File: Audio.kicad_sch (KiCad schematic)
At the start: 25 parts, among them J4 AudioJack3, J5 AudioJack3_SwitchT, U2 MAX9850xTI, U3 TPA6132A2RTE

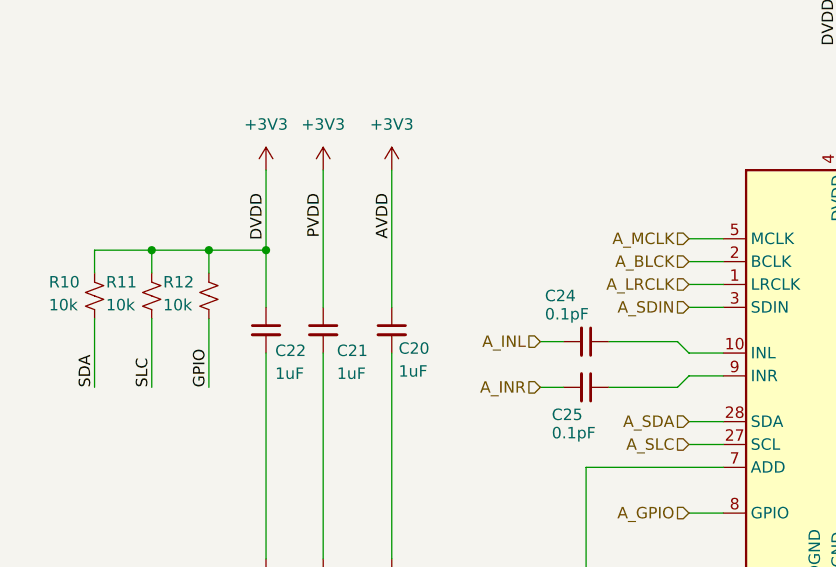
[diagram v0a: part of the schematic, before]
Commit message: Draft 1 - Main components and wiring complete
Connections may be innacurate or violate electrical specs, or perhaps aren't set up "properly".
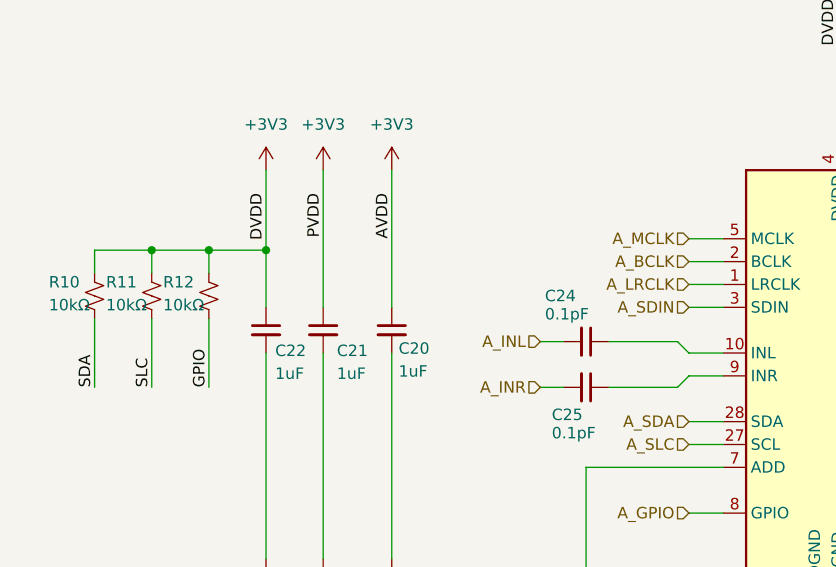
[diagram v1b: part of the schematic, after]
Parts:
- R10, R11, R12: value 10k -> 10kΩ
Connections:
- net A_BLCK renamed A_BCLK
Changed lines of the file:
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@@
 		)
 	)
-	(hierarchical_label "A_BLCK"
+	(hierarchical_label "A_BCLK"
 		(shape input)
 		(at 99.06 71.12 180)
@@
 			)
 		)
-		(property "Value" "10k"
+		(property "Value" "10kΩ"
 			(at 40.64 75.946 0)
 			(effects
@@
 			)
 		)
-		(property "Value" "10k"
+		(property "Value" "10kΩ"
 			(at 34.29 75.946 0)
 			(effects
@@
 			)
 		)
-		(property "Value" "10k"
+		(property "Value" "10kΩ"
 			(at 27.94 75.946 0)
 			(effects

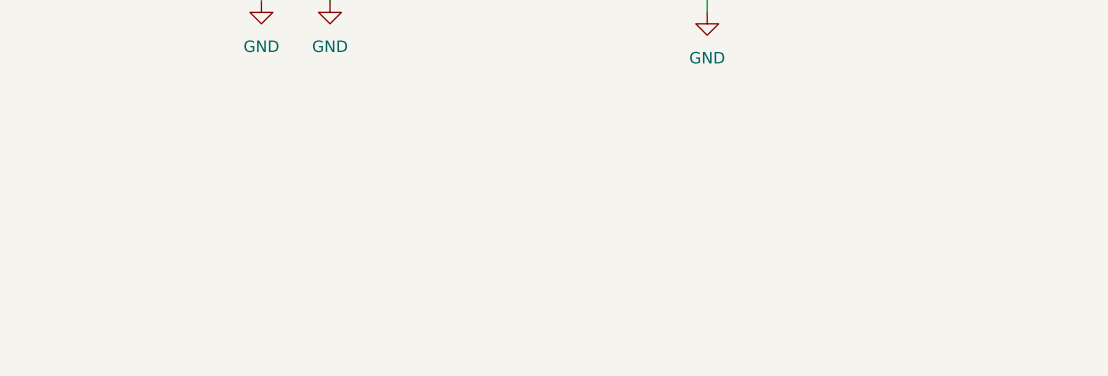
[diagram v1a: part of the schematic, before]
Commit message: Added missing datasheets.
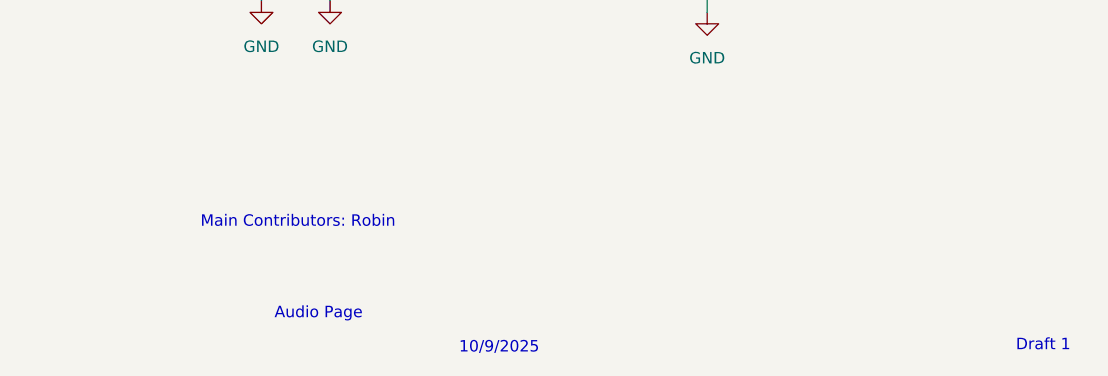
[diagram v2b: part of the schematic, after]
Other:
- note added: "10/9/2025"
- note added: "Audio Page"
- note added: "Draft 1"
- note added: "Main Contributors: Robin"
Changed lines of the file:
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@@
+		)
+	)
+	(text "Audio Page"
+		(exclude_from_sim no)
+		(at 191.77 189.738 0)
+		(effects
+			(font
+				(size 1.27 1.27)
+			)
 		)
 	)
@@
 				(thickness 0.508)
 				(bold yes)
+			)
+		)
+	)
+	(text "Main Contributors: Robin"
+		(exclude_from_sim no)
+		(at 189.484 179.578 0)
+		(effects
+			(font
+				(size 1.27 1.27)
 			)
 		)
@@
 		)
 	)
+	(text "Draft 1"
+		(exclude_from_sim no)
+		(at 272.288 193.294 0)
+		(effects
+			(font
+				(size 1.27 1.27)
+			)
+		)
+	)
 	(text "Place near VDD"
 		(exclude_from_sim no)
@@
 		(effects
 			(font
+				(size 1.27 1.27)
+			)
+		)
+	)
+	(text "10/9/2025"
+		(exclude_from_sim no)
+		(at 211.836 193.548 0)
+		(effects
+			(font

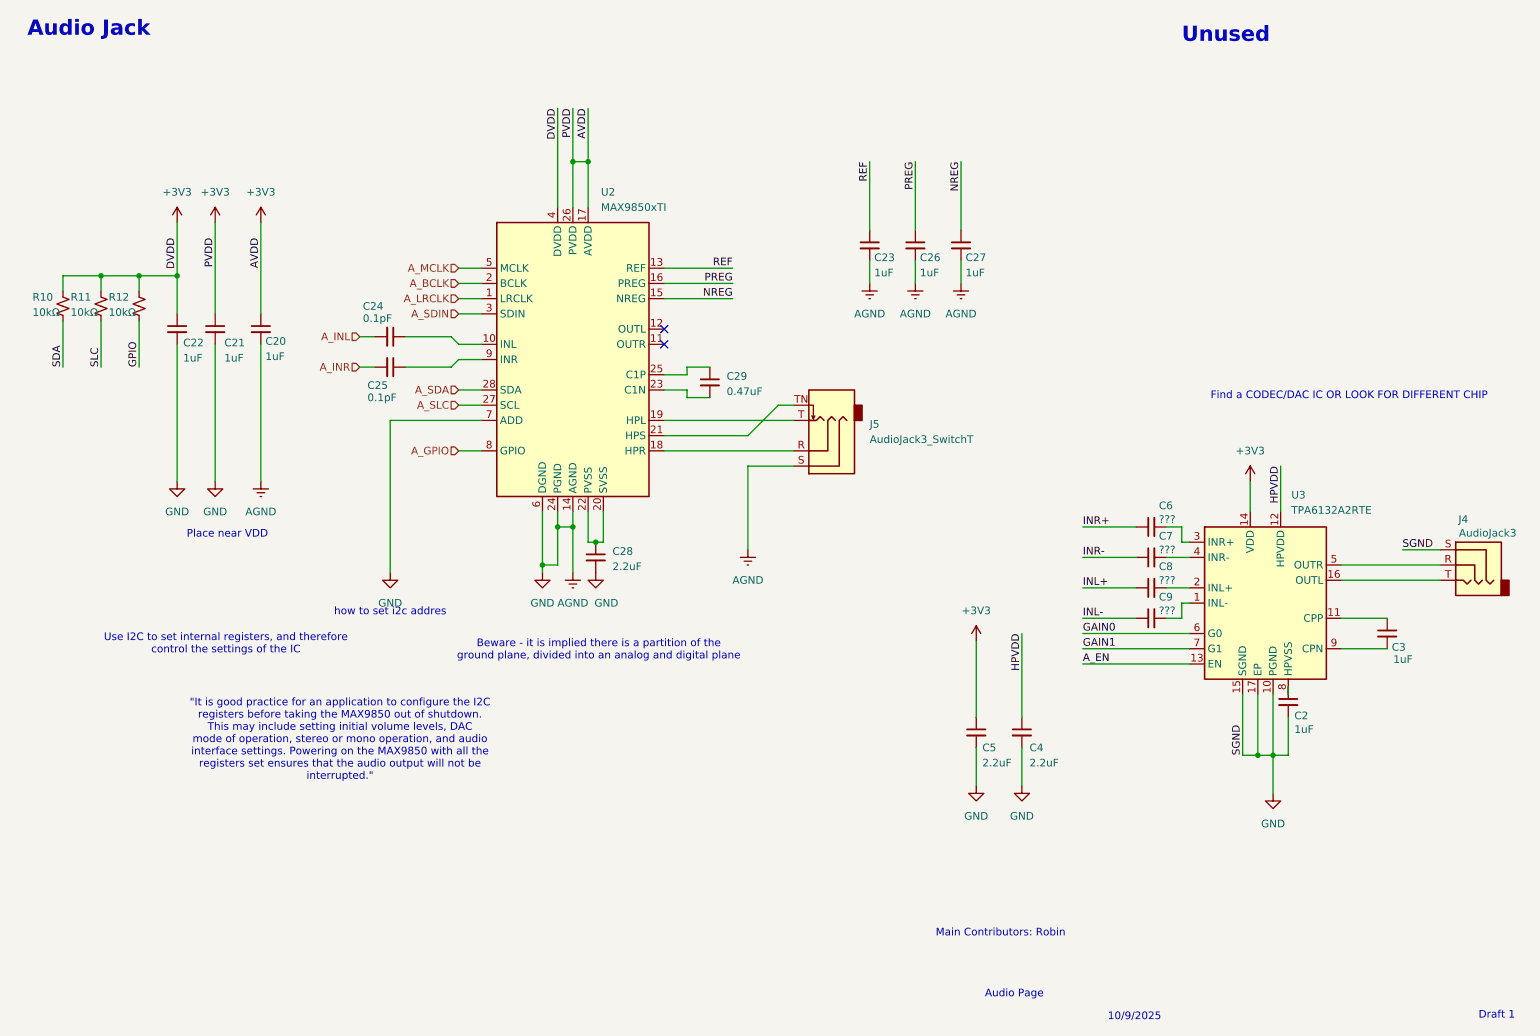
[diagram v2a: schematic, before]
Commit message: Added PMOS to battery + power flags
Still missing values for a lot of components
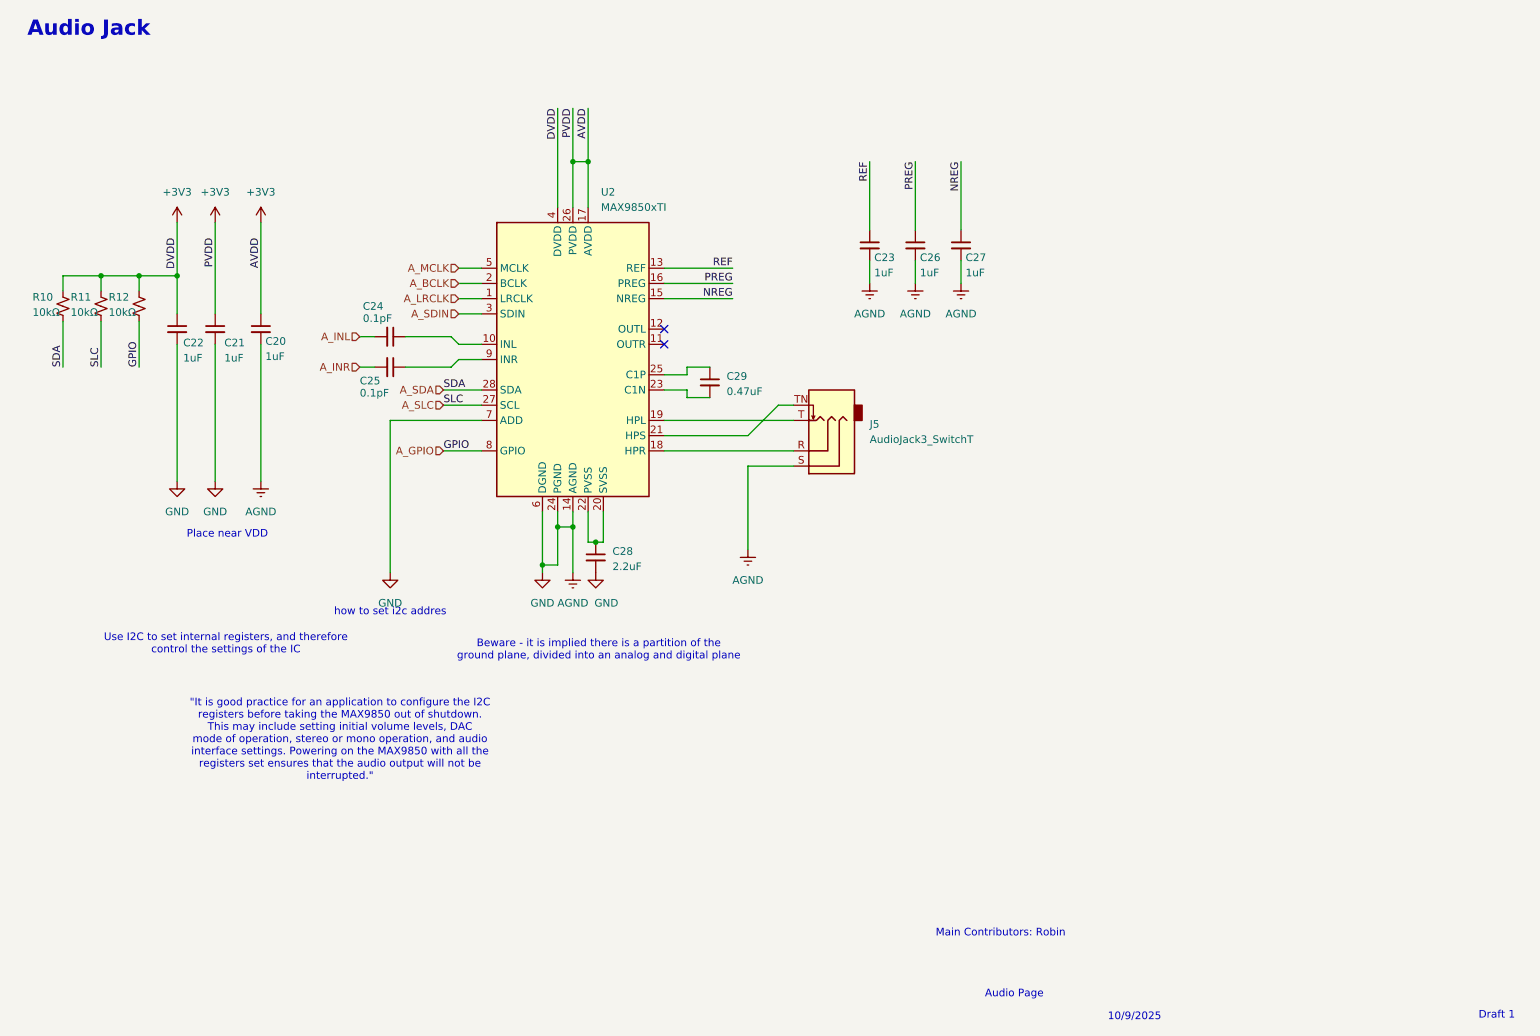
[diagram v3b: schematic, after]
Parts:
- removed C2, C3: 1uF, symbol Device:C_Small
- removed C4, C5: 2.2uF, symbol Device:C_Small
- removed C6, C7, C8, C9: ???, symbol Device:C_Small
- removed J4: AudioJack3, symbol Connector_Audio:AudioJack3
- removed U3: TPA6132A2RTE, Package_DFN_QFN:WQFN-16-1EP_3x3mm_P0.5mm_EP1.6x1.6mm_ThermalVias, symbol Amplifier_Audio:TPA6132A2RTE
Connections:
- net GPIO is gone; now on net A_GPIO: R12.2
- net SDA is gone; now on net A_SDA: R10.2
- net SLC is gone; now on net A_SLC: R11.2
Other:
- note removed: "Find a CODEC/DAC IC OR LOOK FOR DIFFERENT CHIP"
- note removed: "Unused"

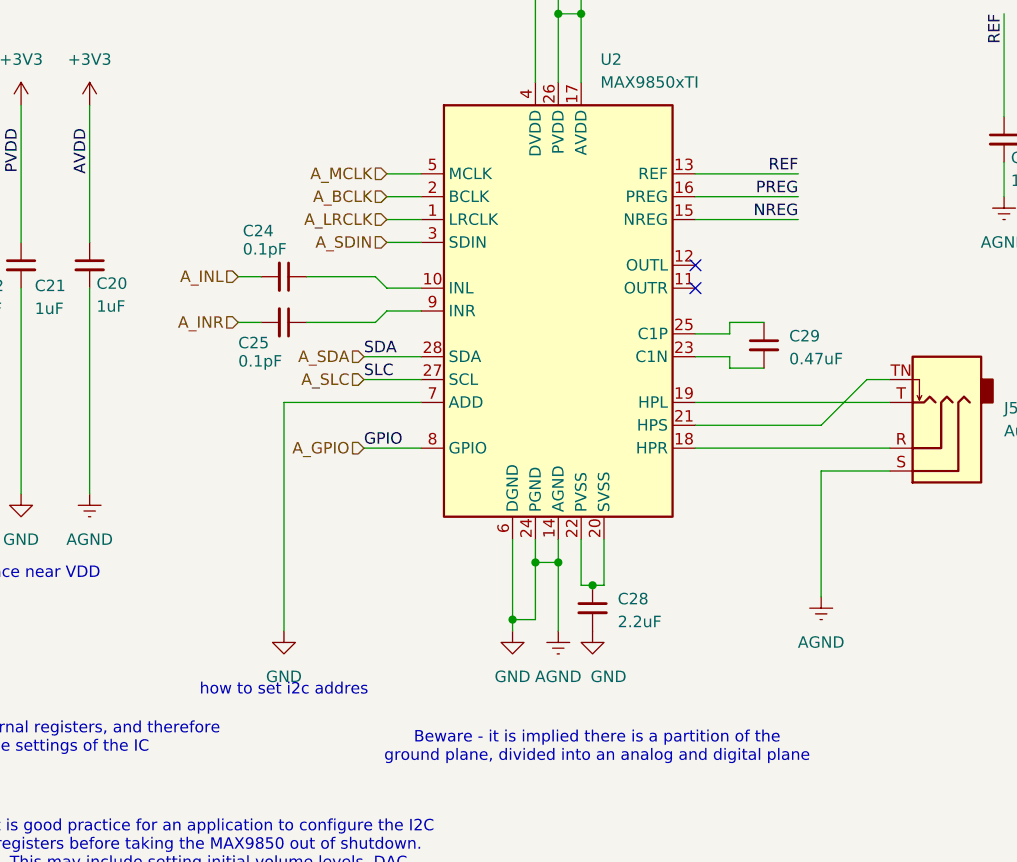
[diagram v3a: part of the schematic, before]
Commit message: Draft 2: Protection circuitry and fixed I/O signals
Still missing PMOS spec for reverse polarity battery protection. Added TVS to USB, voltage divided certain output signals from ICs into ESP GPIO. Checked some component values.
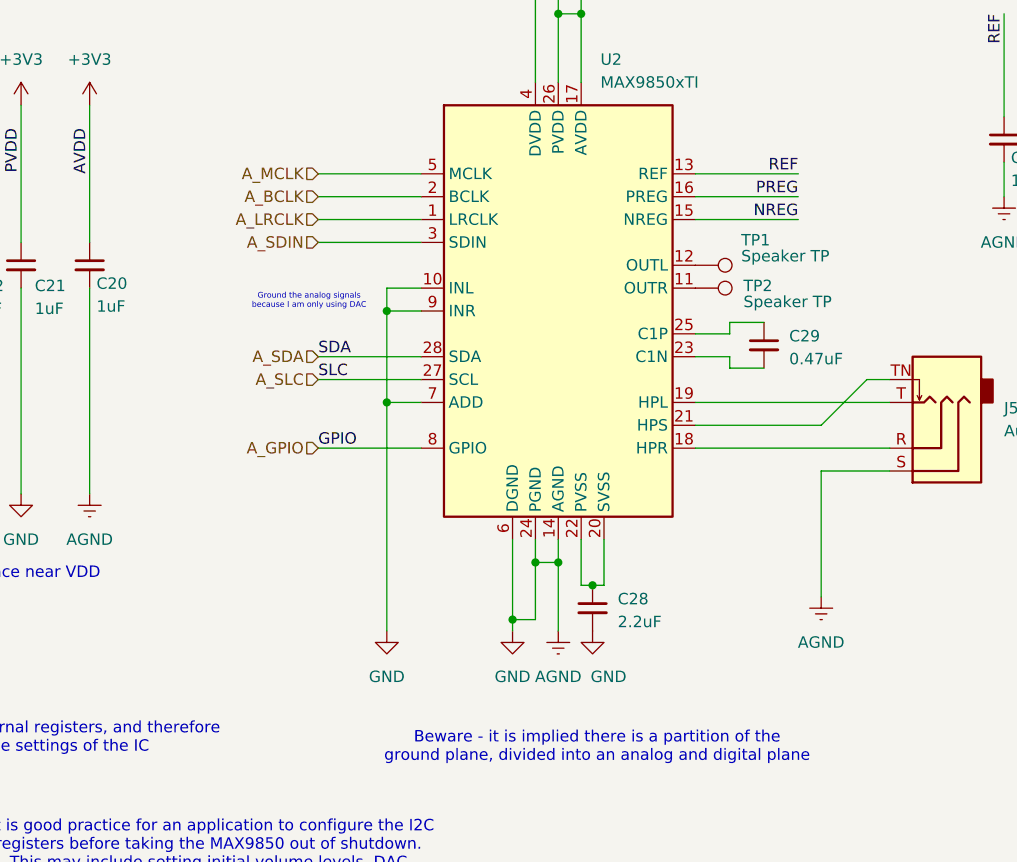
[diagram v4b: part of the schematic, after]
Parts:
- removed C24, C25: 0.1pF, symbol Device:C_Small
- added TP1, TP2: Speaker TP, symbol Connector:TestPoint
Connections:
- net AGND: now also U2.10 (INL), U2.9 (INR)
- net at U2.11 (OUTR): now also TP2.1
- net at U2.12 (OUTL): now also TP1.1
- no-connect marks 2 -> 0
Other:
- note added: "Ground the analog signals because I am only using DAC"
- note removed: "how to set i2c addres"
